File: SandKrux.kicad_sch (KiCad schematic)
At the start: 110 parts, among them CN2 1.25mm-2P socket, IC1 TROPIC01_chip, Q1 S8050, Q2 SI2301CDS-T1-GE3, SW1 TL3330AF130QG, SW2 TL3330AF130QG, SW3 TL3330AF130QG, SW4 TL3330AF130QG, SW5 TL3330AF130QG, U10 AXP173_C3345106, U11 GD32F150G8U6, U2 MT9700, U3 PCIE-67P42H, U9 HX TF-CARD XG8P H1.5, X2 X322526MMB4SI

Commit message: posicionamento de vias e tracos entre os componentes
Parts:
- removed U3: PCIE-67P42H, easyeda2kicad:PCIE-SMD_75P-P0.50_HYC01B-05NGFF-420, symbol easyeda2kicad:PCIE-67P42H
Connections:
- net GND: now also SW1.2, SW1.3, SW1.4
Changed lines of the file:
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@@
 	)
 	(junction
+		(at 551.18 96.52)
+		(diameter 0)
+		(color 0 0 0 0)
+	)
+	(junction
 		(at 457.2 54.61)
 		(diameter 0)
@@
 	(wire
 		(pts
-			(xy 551.18 96.52) (xy 551.18 97.79)
-		)
-		(stroke
-			(width 0)
-			(type default)
-		)
-	)
-	(wire
-		(pts
 			(xy 447.04 148.59) (xy 449.58 148.59)
 		)
@@
 	(wire
 		(pts
+			(xy 551.18 93.98) (xy 551.18 96.52)
+		)
+		(stroke
+			(width 0)
+			(type default)
+		)
+	)
+	(wire
+		(pts
 			(xy 461.01 54.61) (xy 461.01 53.34)
 		)
@@
 	(wire
 		(pts
+			(xy 551.18 96.52) (xy 551.18 99.06)
+		)
+		(stroke
+			(width 0)
+			(type default)
+		)
+	)
+	(wire
+		(pts
 			(xy 499.11 52.07) (xy 499.11 54.61)
 		)
@@
 					(unit 1)
 				)
-			)
-		)
-	)
-	(symbol
-		(lib_id "easyeda2kicad:PCIE-67P42H")
-		(at 121.92 201.93 0)
-		(unit 1)
-		(exclude_from_sim no)
-		(in_bom yes)
-		(on_board yes)
-		(dnp no)
-		(fields_autoplaced yes)
-		(property "Reference" "U3"
-			(at 124.0633 147.32 0)
-			(effects
-				(font
-					(size 1.27 1.27)
-				)
-				(justify left)
-			)
-		)
-		(property "Value" "PCIE-67P42H"
-			(at 124.0633 149.86 0)
-			(effects
-				(font
-					(size 1.27 1.27)
-				)
-				(justify left)
-			)
-		)
-		(property "Footprint" "easyeda2kicad:PCIE-SMD_75P-P0.50_HYC01B-05NGFF-420"
-			(at 121.92 261.62 0)
-			(effects
-				(font
-					(size 1.27 1.27)
-				)
-				(hide yes)
-			)
-		)
-		(property "Datasheet" ""
-			(at 121.92 201.93 0)
-			(effects
-				(font
-					(size 1.27 1.27)
-				)
-				(hide yes)
-			)
-		)
-		(property "Description" ""
-			(at 121.92 201.93 0)
-			(effects
-				(font
-					(size 1.27 1.27)
-				)
-				(hide yes)
-			)
-		)
-		(property "LCSC Part" "C19188865"
-			(at 121.92 264.16 0)
-			(effects
-				(font
-					(size 1.27 1.27)
-				)
-				(hide yes)
-			)
-		)
-		(pin "23"
-		)
-		(pin "33"
-		)
-		(pin "3"
-		)
-		(pin "51"
-		)
-		(pin "57"
-		)
-		(pin "63"
-		)
-		(pin "31"
-		)
-		(pin "71"
-		)
-		(pin "61"
-		)
-		(pin "7"
-		)
-		(pin "45"
-		)
-		(pin "27"
-		)
-		(pin "43"
-		)
-		(pin "39"
-		)
-		(pin "35"
-		)
-		(pin "65"
-		)
-		(pin "37"
-		)
-		(pin "49"
-		)
-		(pin "55"
-		)
-		(pin "5"
-		)
-		(pin "21"
-		)
-		(pin "25"
-		)
-		(pin "9"
-		)
-		(pin "11"
-		)
-		(pin "1"
-		)
-		(pin "29"
-		)
-		(pin "41"
-		)
-		(pin "47"
-		)
-		(pin "53"
-		)
-		(pin "59"
-		)
-		(pin "67"
-		)
-		(pin "69"
-		)
-		(pin "36"
-		)
-		(pin "38"
-		)
-		(pin "44"
-		)
-		(pin "20"
-		)
-		(pin "73"
-		)
-		(pin "4"
-		)
-		(pin "32"
-		)
-		(pin "77"
-		)
-		(pin "52"
-		)
-		(pin "24"
-		)
-		(pin "76"
-		)
-		(pin "2"
-		)
-		(pin "10"
-		)
-		(pin "75"
-		)
-		(pin "6"
-		)
-		(pin "8"
-		)
-		(pin "22"
-		)
-		(pin "26"
-		)
-		(pin "28"
-		)
-		(pin "34"
-		)
-		(pin "30"
-		)
-		(pin "40"
-		)
-		(pin "42"
-		)
-		(pin "46"
-		)
-		(pin "48"
-		)
-		(pin "50"
-		)
-		(pin "54"
-		)
-		(pin "56"
-		)
-		(pin "68"
-		)
-		(pin "70"
-		)
-		(pin "62"
-		)
-		(pin "66"
-		)
-		(pin "72"
-		)
-		(pin "58"
-		)
-		(pin "60"
-		)
-		(pin "64"
-		)
-		(pin "74"
-		)
-		(instances
-			(project ""
-				(path "/0986b4b2-29ef-45bb-b940-2ffd44ad7a0e"
-					(reference "U3")
-					(unit 1)
-				)

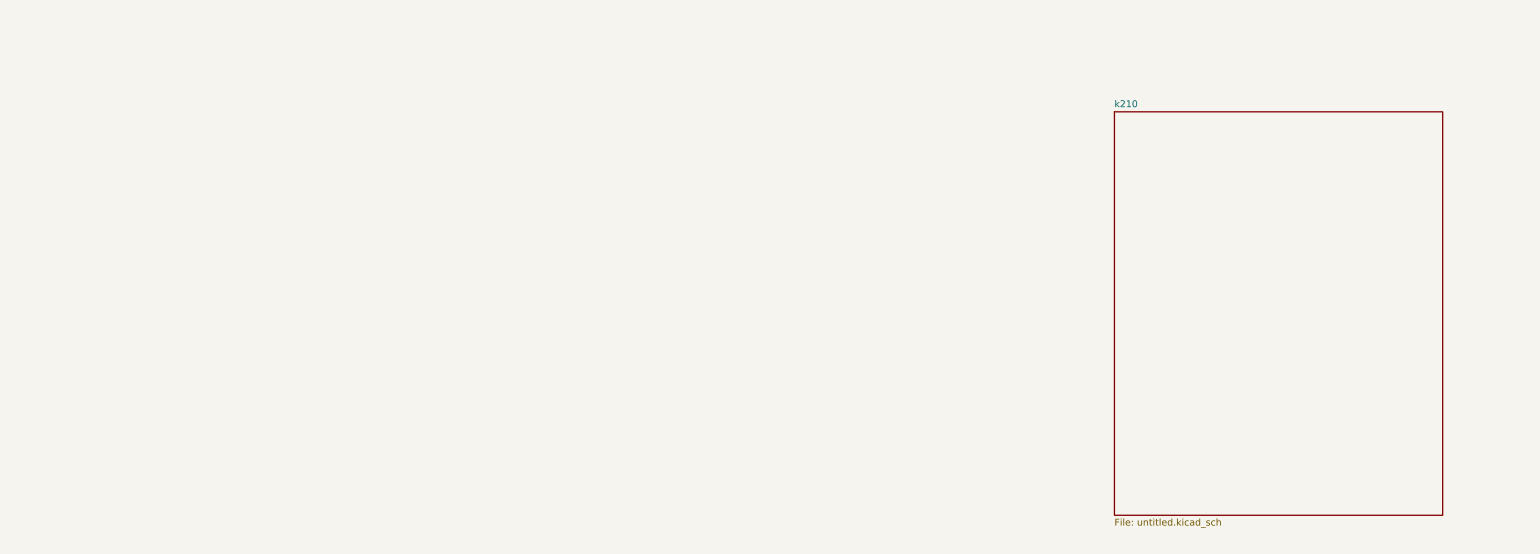
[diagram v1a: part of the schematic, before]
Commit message: m2 conector diagrama na placa principal
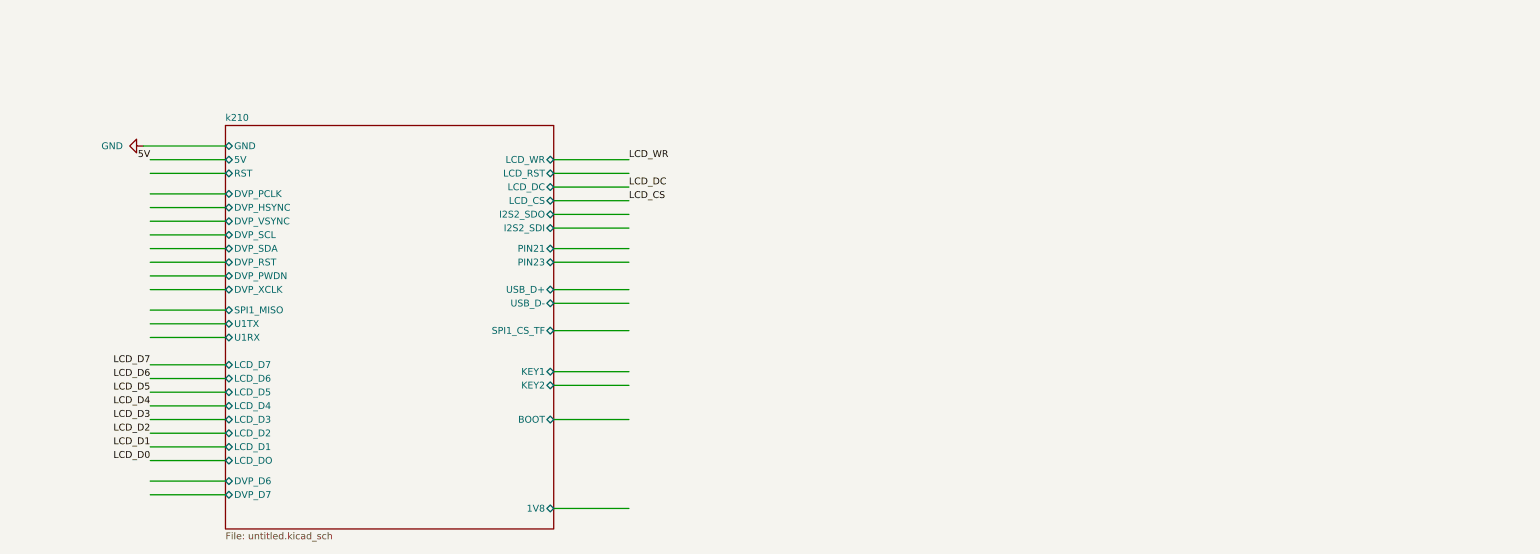
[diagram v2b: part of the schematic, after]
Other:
- sheet k210 ports: added 1V8, 5V, BOOT, DVP_D6, DVP_D7, DVP_HSYNC, DVP_PCLK, DVP_PWDN, DVP_RST, DVP_SCL, DVP_SDA, DVP_VSYNC, DVP_XCLK, GND, I2S2_SDI, I2S2_SDO, KEY1, KEY2, LCD_CS, LCD_D1, LCD_D2, LCD_D3, LCD_D4, LCD_D5, LCD_D6, LCD_D7, LCD_DC, LCD_DO, LCD_RST, LCD_WR, PIN21, PIN23, RST, SPI1_CS_TF, SPI1_MISO, U1RX, U1TX, USB_D+, USB_D-; removed none
